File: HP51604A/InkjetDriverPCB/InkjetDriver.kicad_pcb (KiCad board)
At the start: 2 copper layers, 36.8 x 88.9 mm, 19 parts, among them P1 EXPANSION_HEADER, P2 PWR, P3 INKJET, U1 ee6B595, U2 6B595, U3 LT1072

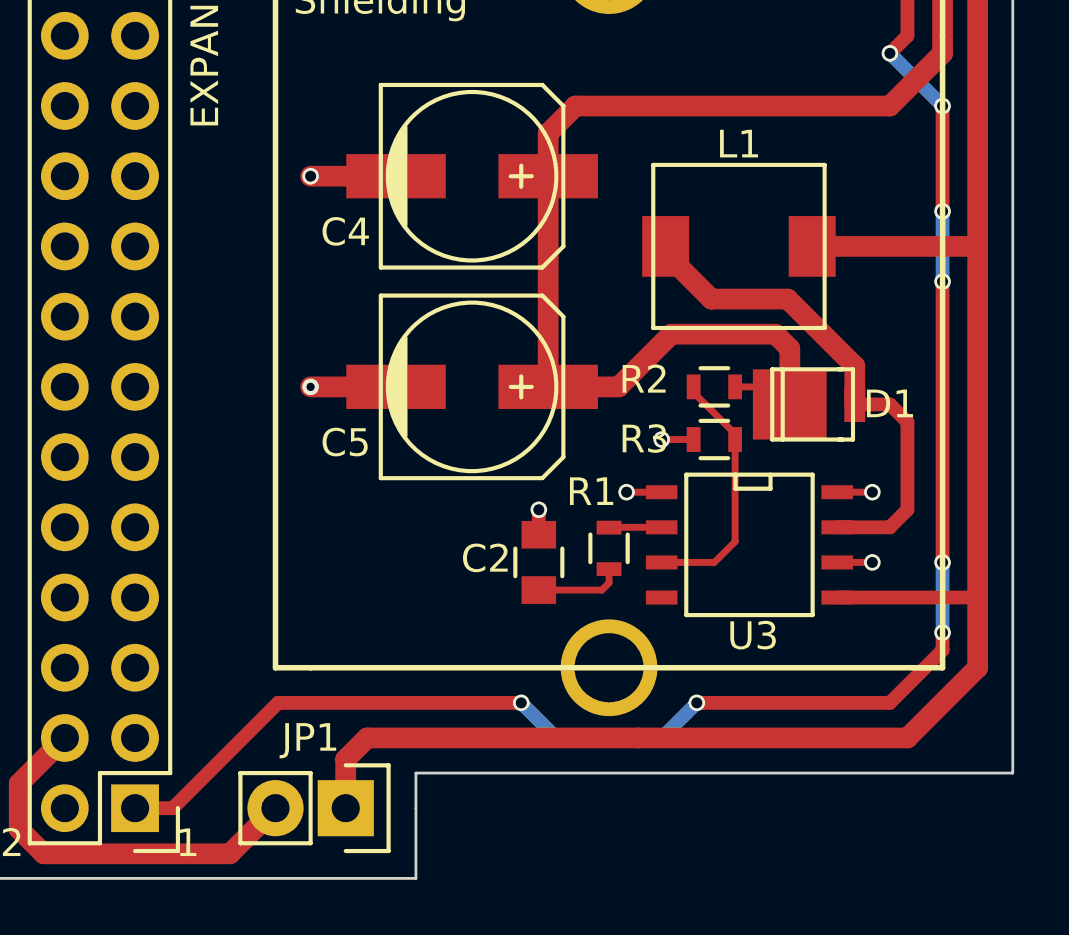
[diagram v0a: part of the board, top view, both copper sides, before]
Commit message: Interface PCB changed to allow 19V supply to be routed past the buck converter.
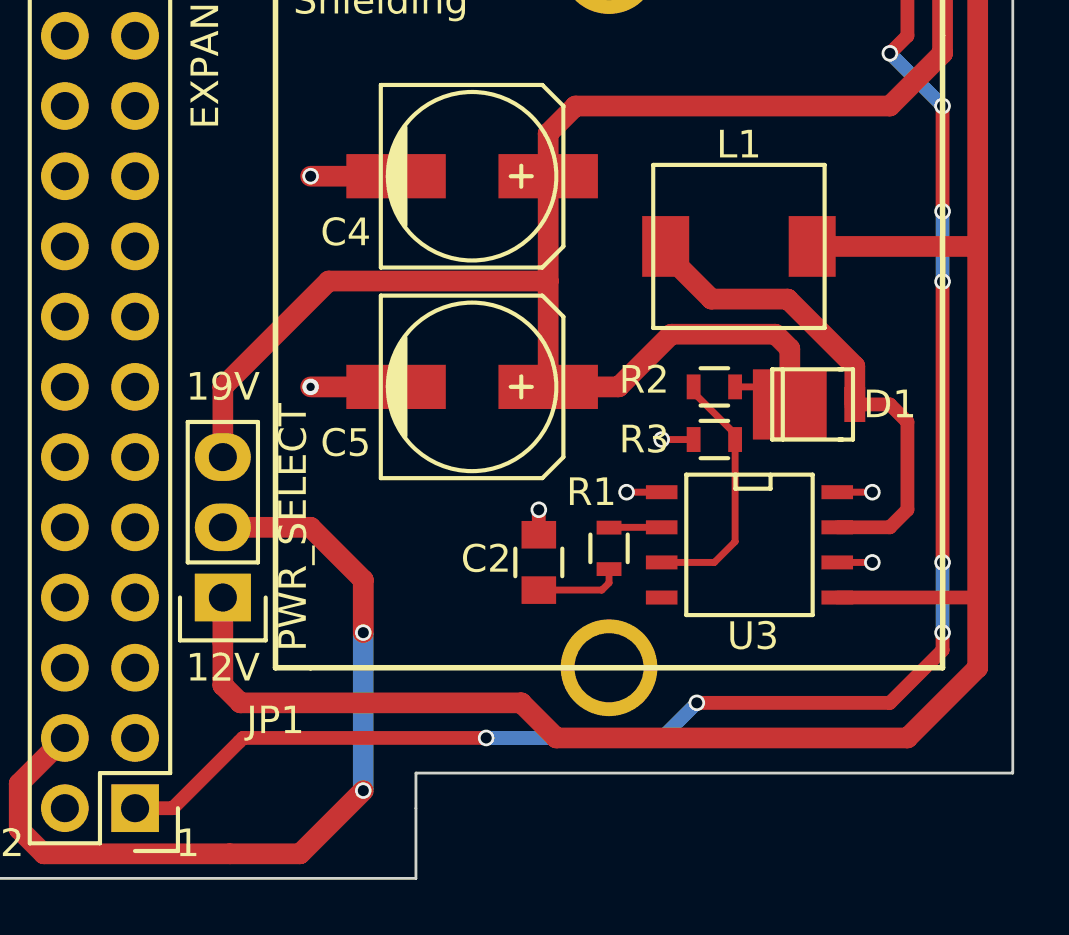
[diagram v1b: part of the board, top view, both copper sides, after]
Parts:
- JP1: value 12V_EN -> PWR_SELECT; footprint Socket_Strips:Socket_Strip_Straight_1x02 -> Socket_Strips:Socket_Strip_Straight_1x03
- U1: value ee6B595 -> 6B595
- moved JP1 8.82 mm to (107.3, 106.7), turned to 90 degrees
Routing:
- net Net-(JP1-Pad2): track 14.3 -> 31.2 mm, vias 0 -> 2
- net 19V: track 136.8 -> 152.7 mm
- net +12V: track 125.7 -> 132.0 mm
- net +5V: track 126.5 -> 125.5 mm
